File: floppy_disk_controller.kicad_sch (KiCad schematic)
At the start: 60 parts, among them J1 Conn_02x18_Odd_Even, U15 L78L05_TO92

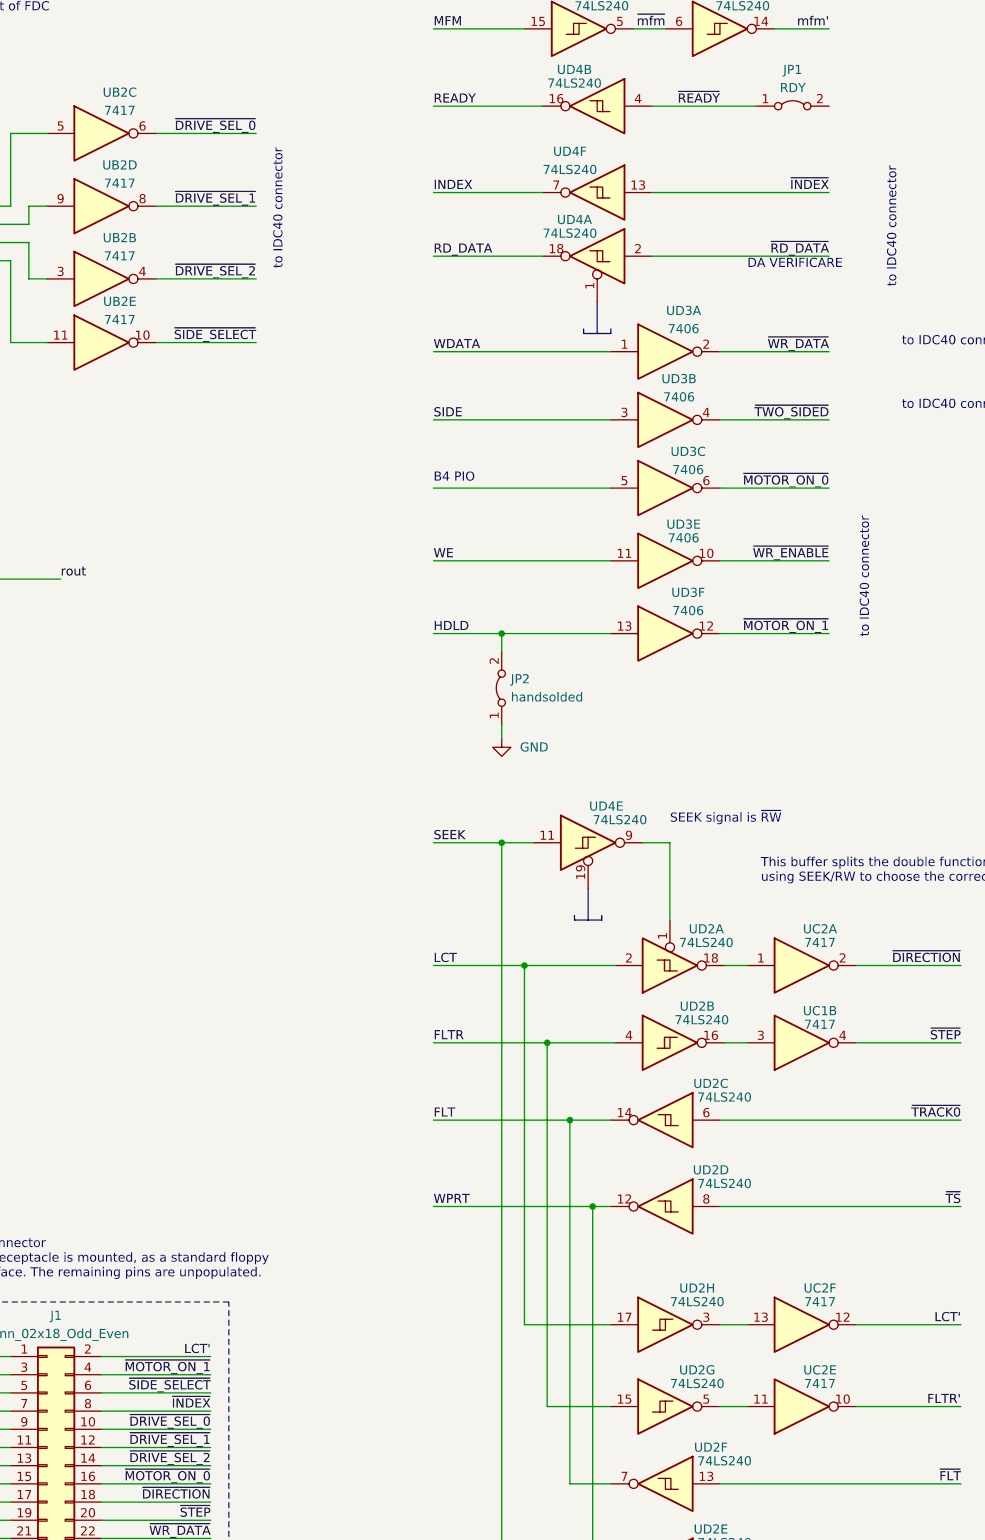
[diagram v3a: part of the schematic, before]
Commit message: Graphical error: 7417 is a non-inverting buffer
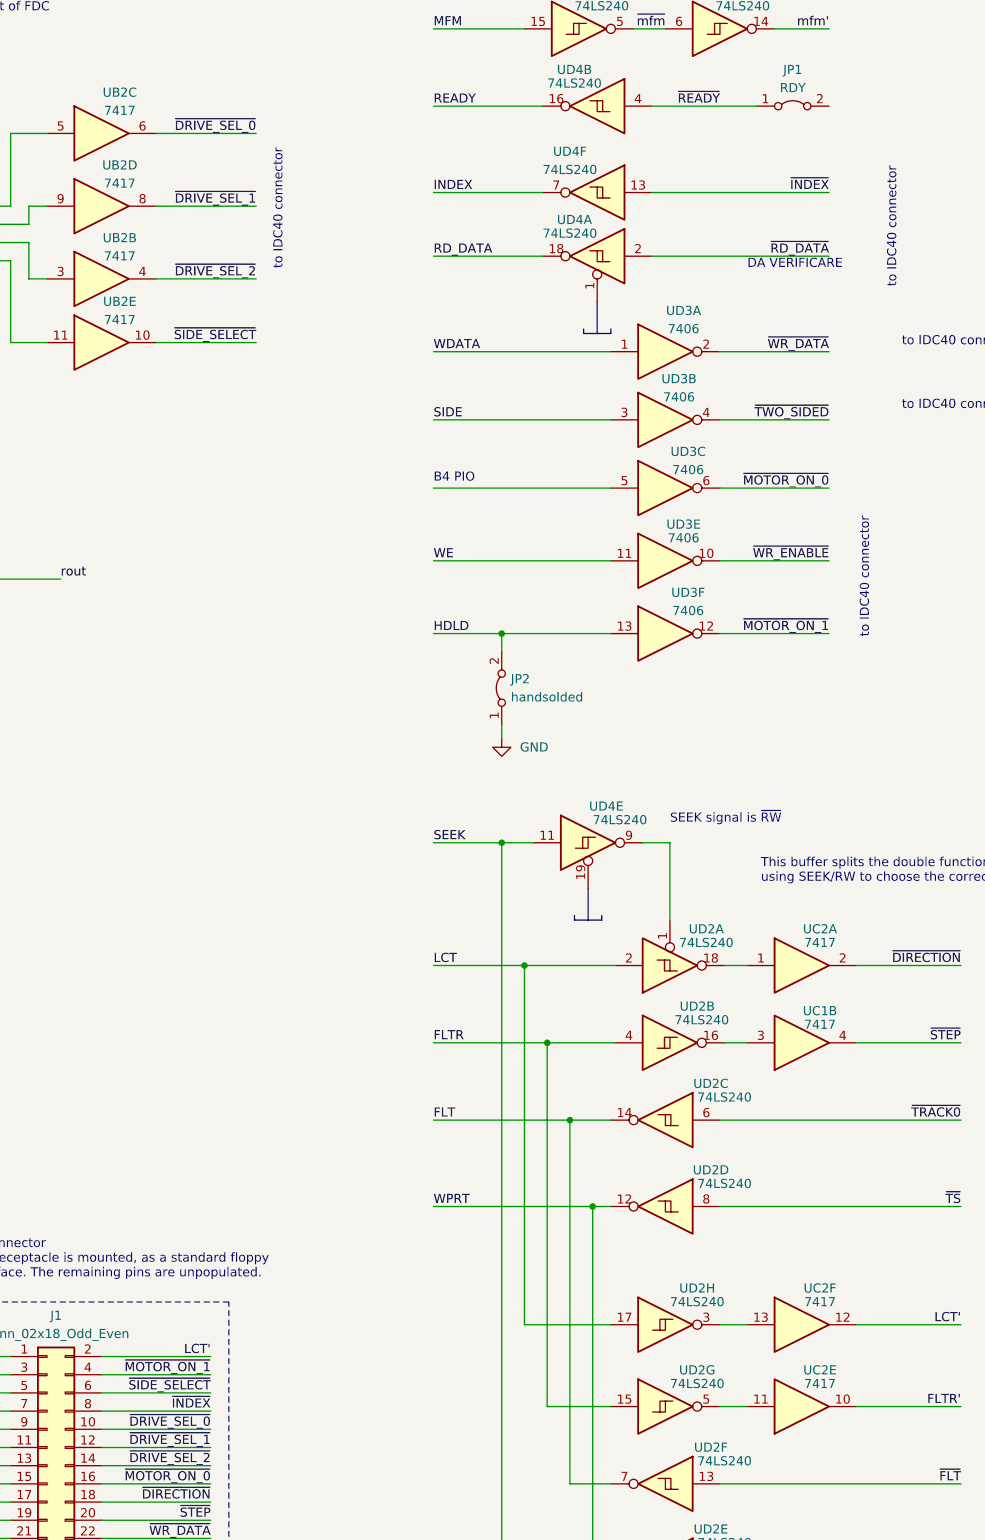
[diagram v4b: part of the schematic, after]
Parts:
- UB2, UC1, UC2: symbol 74xx:74LS04 -> 74xx:74LS07
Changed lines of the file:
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@@
     )
   )
-  (symbol (lib_id "74xx:74LS04") (at 259.08 59.69 0) (unit 2)
+  (symbol (lib_id "74xx:74LS07") (at 259.08 59.69 0) (unit 2)
     (in_bom yes) (on_board yes) (dnp no)
     (property "Reference" "UB2" (at 261.62 53.975 0)
@@
       (effects (font (size 1.27 1.27)) hide)
     )
-    (property "Datasheet" "http://www.ti.com/lit/gpn/sn74LS04" (at 259.08 59.69 0)
+    (property "Datasheet" "www.ti.com/lit/ds/symlink/sn74ls07.pdf" (at 259.08 59.69 0)
       (effects (font (size 1.27 1.27)) hide)
     )
@@
     )
   )
-  (symbol (lib_id "74xx:74LS04") (at 356.87 205.74 0) (unit 6)
+  (symbol (lib_id "74xx:74LS07") (at 356.87 205.74 0) (unit 6)
     (in_bom yes) (on_board yes) (dnp no)
     (property "Reference" "UC2" (at 359.41 200.66 0)
@@
     )
   )
-  (symbol (lib_id "74xx:74LS04") (at 259.08 68.58 0) (unit 5)
+  (symbol (lib_id "74xx:74LS07") (at 259.08 68.58 0) (unit 5)
     (in_bom yes) (on_board yes) (dnp no)
     (property "Reference" "UB2" (at 261.62 62.865 0)
@@
       (effects (font (size 1.27 1.27)) hide)
     )
-    (property "Datasheet" "http://www.ti.com/lit/gpn/sn74LS04" (at 259.08 68.58 0)
+    (property "Datasheet" "www.ti.com/lit/ds/symlink/sn74ls07.pdf" (at 259.08 68.58 0)
       (effects (font (size 1.27 1.27)) hide)
     )
@@
     )
   )
-  (symbol (lib_id "74xx:74LS04") (at 356.87 155.575 0) (unit 1)
+  (symbol (lib_id "74xx:74LS07") (at 356.87 155.575 0) (unit 1)
     (in_bom yes) (on_board yes) (dnp no)
     (property "Reference" "UC2" (at 359.41 150.495 0)
@@
     )
   )
-  (symbol (lib_id "74xx:74LS04") (at 356.87 217.17 0) (mirror x) (unit 5)
+  (symbol (lib_id "74xx:74LS07") (at 356.87 217.17 0) (mirror x) (unit 5)
     (in_bom yes) (on_board yes) (dnp no)
     (property "Reference" "UC2" (at 359.41 212.09 0)
@@
     )
   )
-  (symbol (lib_id "74xx:74LS04") (at 259.08 39.37 0) (unit 3)
+  (symbol (lib_id "74xx:74LS07") (at 259.08 39.37 0) (unit 3)
     (in_bom yes) (on_board yes) (dnp no)
     (property "Reference" "UB2" (at 261.62 33.655 0)
@@
       (effects (font (size 1.27 1.27)) hide)
     )
-    (property "Datasheet" "http://www.ti.com/lit/gpn/sn74LS04" (at 259.08 39.37 0)
+    (property "Datasheet" "www.ti.com/lit/ds/symlink/sn74ls07.pdf" (at 259.08 39.37 0)
       (effects (font (size 1.27 1.27)) hide)
     )
@@
     )
   )
-  (symbol (lib_id "74xx:74LS04") (at 259.08 49.53 0) (unit 4)
+  (symbol (lib_id "74xx:74LS07") (at 259.08 49.53 0) (unit 4)
     (in_bom yes) (on_board yes) (dnp no)
     (property "Reference" "UB2" (at 261.62 43.815 0)
@@
       (effects (font (size 1.27 1.27)) hide)
     )
-    (property "Datasheet" "http://www.ti.com/lit/gpn/sn74LS04" (at 259.08 49.53 0)
+    (property "Datasheet" "www.ti.com/lit/ds/symlink/sn74ls07.pdf" (at 259.08 49.53 0)
       (effects (font (size 1.27 1.27)) hide)
     )
@@
     )
   )
-  (symbol (lib_id "74xx:74LS04") (at 356.87 166.37 0) (mirror x) (unit 2)
+  (symbol (lib_id "74xx:74LS07") (at 356.87 166.37 0) (mirror x) (unit 2)
     (in_bom yes) (on_board yes) (dnp no)
     (property "Reference" "UC1" (at 359.41 161.925 0)

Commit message: Notes in kicad's sheet text blocks
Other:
- company: (none) -> Logic Systems Int'l Inc
- title: (none) -> CEDA - Sanco 8003 schematics
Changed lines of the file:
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@@
 (kicad_sch (version 20230121) (generator eeschema)
   (paper "A3")
+  (title_block
+    (title "CEDA - Sanco 8003 schematics")
+    (rev "05")
+    (company "Logic Systems Int'l Inc")
+    (comment 1 "reversed by RetrOfficina - retrofficina.glgprograms.it")
+    (comment 4 "Floppy Disk Controller")
+  )
   (junction (at 242.57 268.605) (diameter 0) (color 0 0 0 0)
   )

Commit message: FDC: added missing TC wire from small IO to FDC
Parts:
- added unit 5 of UB9
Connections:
- net at UE2.16 (TC): now also UB9.10
- new net ~{FDC_TC}: UB9.11
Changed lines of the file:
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@@
     (stroke (width 0) (type default))
   )
+  (wire (pts (xy 15.24 58.42) (xy 24.13 58.42))
+    (stroke (width 0) (type default))
+  )
   (wire (pts (xy -6.35 167.64) (xy -6.35 166.37))
     (stroke (width 0) (type default))
@@
     (stroke (width 0) (type default))
   )
+  (wire (pts (xy 41.91 67.31) (xy 44.45 67.31))
+    (stroke (width 0) (type default))
+  )
   (wire (pts (xy -16.51 177.8) (xy -16.51 248.92))
     (stroke (width 0) (type default))
@@
     (stroke (width 0) (type default))
   )
+  (wire (pts (xy 39.37 58.42) (xy 41.91 58.42))
+    (stroke (width 0) (type default))
+  )
   (wire (pts (xy 167.64 237.49) (xy 176.53 237.49))
     (stroke (width 0) (type default))
@@
     (stroke (width 0) (type default))
   )
+  (wire (pts (xy 41.91 58.42) (xy 41.91 67.31))
+    (stroke (width 0) (type default))
+  )
   (wire (pts (xy -50.8 167.64) (xy -50.8 166.37))
     (stroke (width 0) (type default))
@@
     (effects (font (size 1.27 1.27)) (justify left bottom))
   )
+  (label "~{FDC_TC}" (at 15.24 58.42 0) (fields_autoplaced)
+    (effects (font (size 1.27 1.27)) (justify left bottom))
+  )
   (label "WDATA" (at 305.435 69.85 0) (fields_autoplaced)
     (effects (font (size 1.27 1.27)) (justify left bottom))
@@
   )
   (symbol (lib_id "Device:R") (at 22.86 72.39 90) (unit 1)
-    (in_bom yes) (on_board yes) (dnp no) (fields_autoplaced)
+    (in_bom yes) (on_board yes) (dnp no)
     (property "Reference" "R82" (at 22.86 66.04 90)
       (effects (font (size 1.27 1.27)))
@@
         )
       )
+    )
+  )
+  (symbol (lib_id "74xx:74LS04") (at 31.75 58.42 0) (unit 5)
+    (in_bom yes) (on_board yes) (dnp no) (fields_autoplaced)
+    (property "Reference" "UB9" (at 31.75 49.53 0)
+      (effects (font (size 1.27 1.27)))
+    )
+    (property "Value" "74LS04" (at 31.75 52.07 0)
+      (effects (font (size 1.27 1.27)))
+    )
+    (property "Footprint" "" (at 31.75 58.42 0)
+      (effects (font (size 1.27 1.27)) hide)
+    )
+    (property "Datasheet" "http://www.ti.com/lit/gpn/sn74LS04" (at 31.75 58.42 0)
+      (effects (font (size 1.27 1.27)) hide)
+    )
+    (pin "1")
+    (pin "2")
+    (pin "3")
+    (pin "4")
+    (pin "5")
+    (pin "6")
+    (pin "8")
+    (pin "9")
+    (pin "10")
+    (pin "11")
+    (pin "12")
+    (pin "13")
+    (pin "14")
+    (pin "7")
+    (instances
+      (project "ceda"
+        (path "/12a6dbe3-008d-4c5b-88f6-9f1c816060be/30cc577a-62cc-4eb0-beb7-81a864bc3256"
+          (reference "UB9") (unit 5)
+        )
+      )

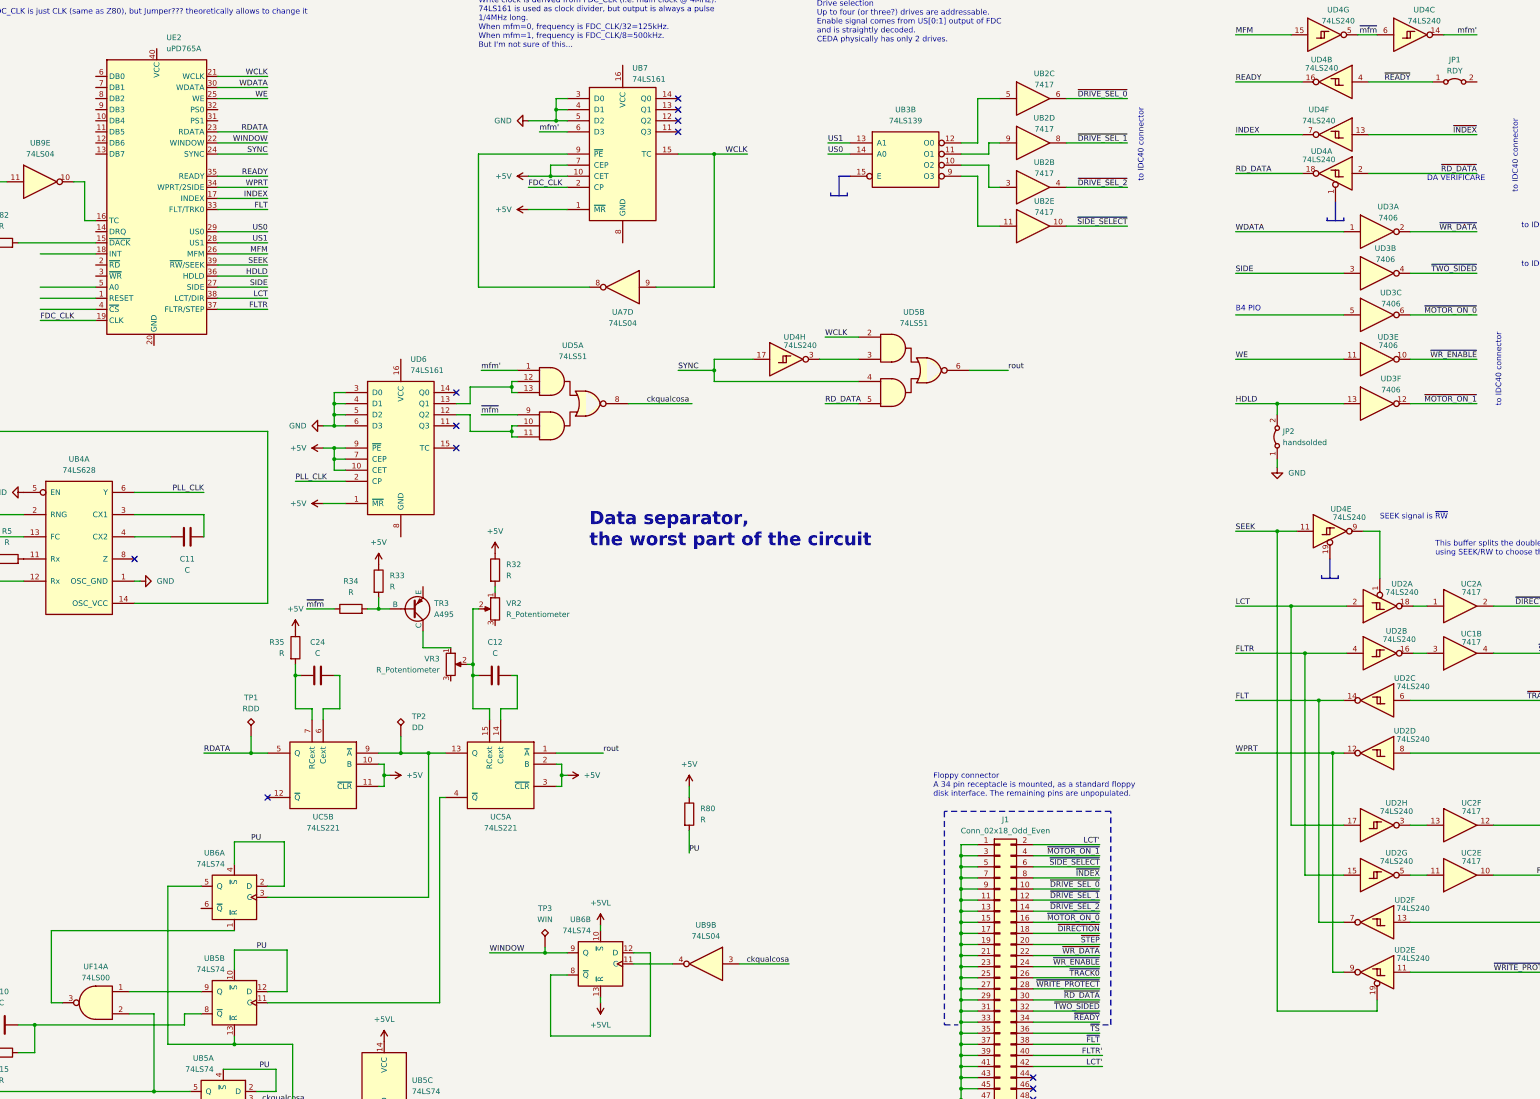
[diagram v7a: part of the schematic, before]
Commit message: Upgrade to KiCAD 9.0
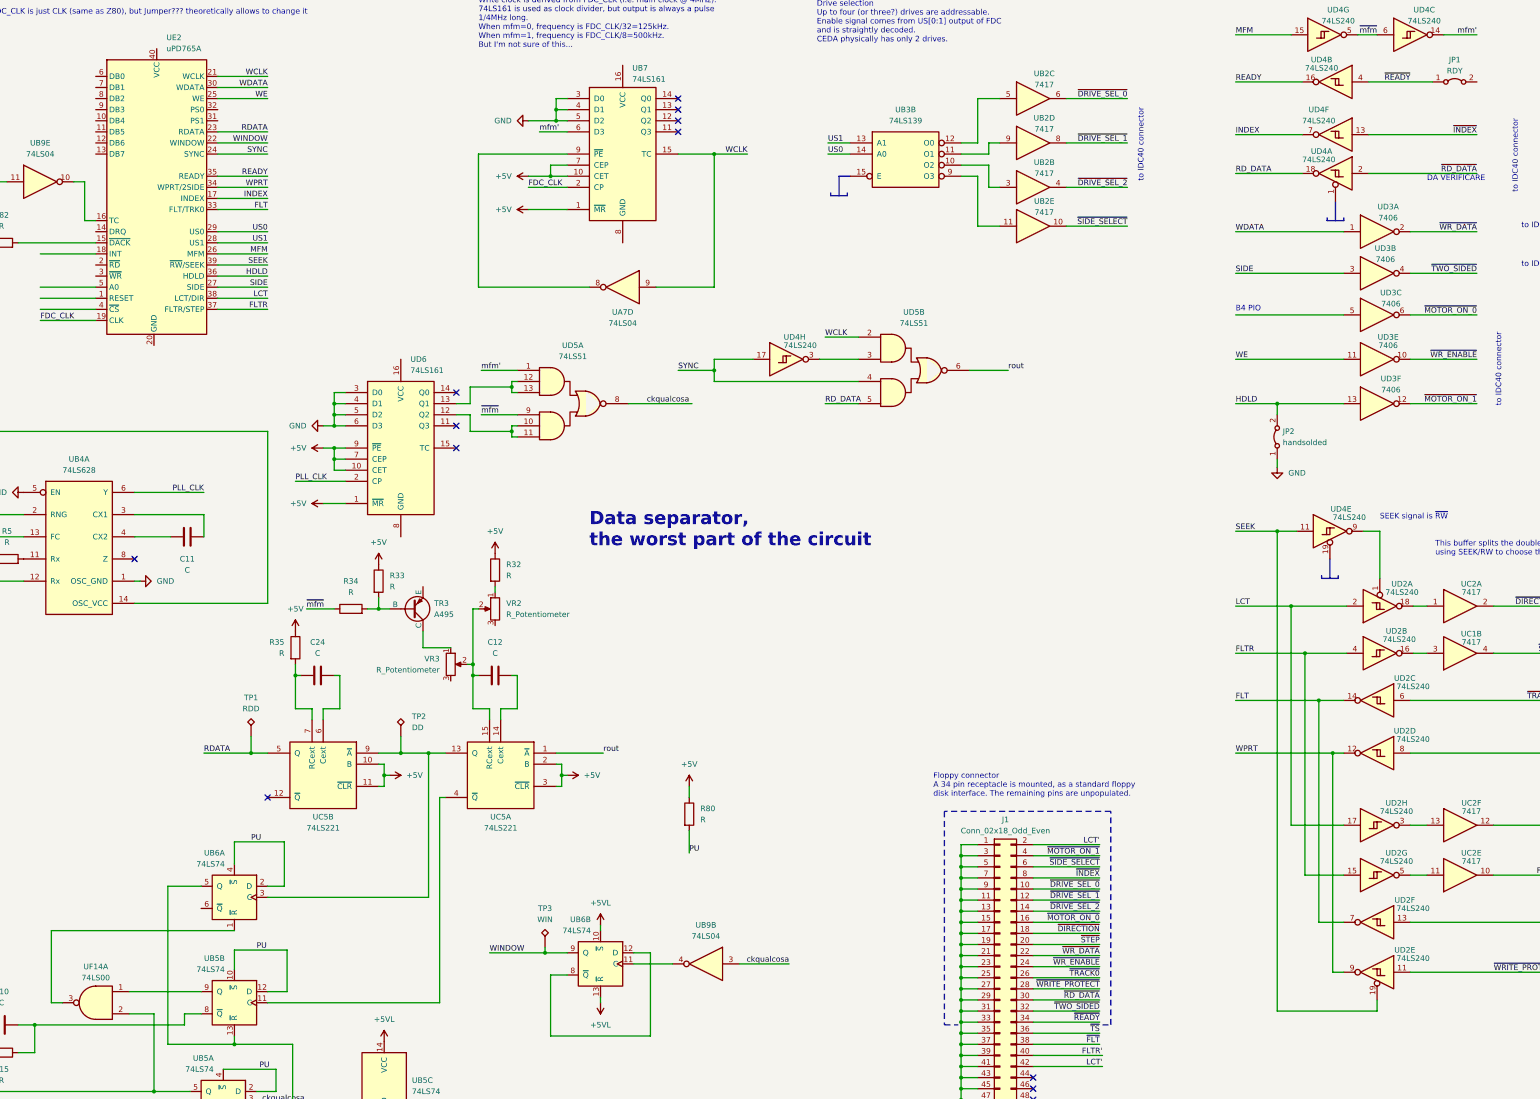
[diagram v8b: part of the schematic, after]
